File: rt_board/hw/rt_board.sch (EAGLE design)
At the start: 66 parts, among them IC1 MCP170333MB, IC2/L1 TLE4935L, IC3/L2 TLE4935L, IC4/L1 TLE4935L, IC5/L2 TLE4935L, Q1 8MHz, SW1 B3U-1000PM-B, SW2 B3U-1000PM-B, U1 STM32F051R8T7, U2 SN74AVC4T245PW, U3 DRV8801PWP, U4 ACS712ELCTR-05B-T, U5 DRV8801PWP, U6 ACS712ELCTR-05B-T, U7 2N7002BKW, X1 PWR, X2 LEFT, X3 RIGHT

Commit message: first PCB/SMD version
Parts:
- removed D3: BZX84CSMD, diode:BZX84CSMD
- C12: value 100uF -> 100nF; device rcl:CPOL-EU153CLV-0810 -> rcl:C-EUC1206
- C14: value 1nF -> 20pF; device rcl:C-EUC1206 -> rcl:C-EUC0603
- C15: value 100nF -> 100uF; device rcl:C-EUC1206 -> rcl:CPOL-EU153CLV-0605
- C16: value 100nF -> 20pF; device rcl:C-EUC1206 -> rcl:C-EUC0603
- C18: value 100uF -> 4.7uF; device rcl:CPOL-EU153CLV-0810 -> rcl:CPOL-EU153CLV-0405
- C2: value 4.7uF -> 100nF; device rcl:CPOL-EU153CLV-0405 -> rcl:C-EUC1206
- C20: value 1nF -> 100nF
- C22: value 100nF -> 4.7uF; device rcl:C-EUC1206 -> rcl:CPOL-EU153CLV-0405
- C3: device rcl:CPOL-EU153CLV-0605 -> rcl:CPOL-EU153CLV-0810
- C4: value 4.7uF -> 100uF; device rcl:CPOL-EU153CLV-0405 -> rcl:CPOL-EU153CLV-0810
- C7: value 100nF -> 1nF
- C8: value 20pF -> 1nF; device rcl:C-EUC0603 -> rcl:C-EUC1206
- C9: value 20pF -> 100nF; device rcl:C-EUC0603 -> rcl:C-EUC1206
- D1: value CGRM4001-G -> BZX84CSMD; device diode:CGRM4001-G -> diode:BZX84CSMD
- R1, R2: value 1kR -> 2kR
- R10: value 3kR -> 3.3kR
- R11: value 3.3kR -> 350mA; device rcl:R-EU_R0603 -> rcl:R-EU_MELF0204W
- R12: value 2kR -> 350mA; device rcl:R-EU_R0603 -> rcl:R-EU_MELF0204W
- R13: value 3kR -> 1kR
- R14: value 2kR -> 1kR
- R15: value 3kR -> 100kR
- R16: value 3.3kR -> 100kR
- R3, R4: value 100kR -> 2kR
- R5, R6: value 350mA -> 3kR; device rcl:R-EU_MELF0204W -> rcl:R-EU_R0603
- R7: value 2kR -> 3kR
- R9: value 2kR -> 3.3kR
- U1: value STM32F051R8T7 -> DRV8801PWP; device stm32f51r8r6:STM32F051R8T6 -> TI-DRV8801PWP:DRV8801PWP
- U2: value SN74AVC4T245PW -> DRV8801PWP; device TI-SN74AVC4T245PW:SN74AVC4T245PW -> TI-DRV8801PWP:DRV8801PWP
- U3: value DRV8801PWP -> SN74AVC4T245PW; device TI-DRV8801PWP:DRV8801PWP -> TI-SN74AVC4T245PW:SN74AVC4T245PW
- U5: value DRV8801PWP -> ACS712ELCTR-05B-T; device TI-DRV8801PWP:DRV8801PWP -> Allegro-ACS712ELCTR-20A-T:ACS712ELCTR-20A-T
- U6: value ACS712ELCTR-05B-T -> STM32F051R8T7; device Allegro-ACS712ELCTR-20A-T:ACS712ELCTR-20A-T -> stm32f51r8r6:STM32F051R8T6
- X1: value PWR -> LEFT
- X2: value LEFT -> RIGHT
- X3: value RIGHT -> PWR
- renumbered IC3/L2 to IC3/L1, IC5/L2 to IC5/L1
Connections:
- removed net N$1: C3.+, D1.C, IC1.VI1
- net +12V: now also C1.1, C12.1, C2.1, C3.+, C4.+, U1.VBB, U2.VBB; no longer C12.+, C15.1, C17.1, C18.+, C21.1, U3.VBB, U5.VBB
- net +5V: now also C18.+, C19.1, C20.1, C21.1, C22.+, R14.1, R15.2, U3.VCCB, U6.VBAT, U6.VDD, U6.VDD_2; no longer C1.1, C2.+, C4.+, C5.1, C6.1, R2.1, R4.2, U1.VBAT, U1.VDD, U1.VDD_2, U2.VCCB
- net +5V/1: now also C15.+, C5.1, C6.1, IC1.VI1, R12.2, U5.VCC; no longer C13.1, C19.1, D1.A, R6.2, U6.VCC
- net +5V/4: now also R10.2, R11.1, R9.2, U3.1DIR, U3.VCCA; no longer R11.2, R16.2, R5.1, U2.1DIR, U2.VCCA
- net 0V: now also C15.-, C16.2, C2.2, C21.2, C22.-, D1.A, R13.1, R16.1, R5.2, R6.2, R7.2, U1.EP, U1.GND, U1.GND_2, U1.MODE_2, U2.EP, U2.MODE_2, U3.1~OE, U3.2DIR, U3.2~OE, U5.IP-, U5.IP-_2, U6.VSS, U6.VSSA, U6.VSS_2, X3-2.KL; no longer C10.2, C11.2, C12.-, C2.-, C9.2, D3.A, R1.1, R10.2, R13.2, R15.2, R3.1, U1.VSS, U1.VSSA, U1.VSS_2, U2.1~OE, U2.2DIR, U2.2~OE, U3.EP, U3.MODE_2, U5.EP, U5.GND_2, U5.MODE_2, U6.GND, U6.IP-, U6.IP-_2, X1-2.KL
- net N$10: now also R12.1; no longer R6.1
- net N$11: now also R11.2; no longer R5.2
- net N$12: now also U3.1A1; no longer U2.1A1
- net N$13: now also U3.1B1, U6.PA3; no longer U1.PA3, U2.1B1
- net N$14: now also U3.2B1, U6.PA2; no longer U1.PA2, U2.2B1
- net N$15: now also U3.2A1; no longer U2.2A1
- net N$16: now also R1.1; no longer R7.1
- net N$17: now also R1.2, R5.1, U6.PA8; no longer R7.2, R8.1, U1.PA8
- net N$18: now also R2.1; no longer R9.1
- net N$19: now also R2.2, R6.1, U6.PA9; no longer R10.1, R9.2, U1.PA9
- net N$2: now also X3-1.KL; no longer X1-1.KL
- net N$20: now also U1.OUT+, X1-1.KL; no longer U3.OUT+, X2-1.KL
- net N$21: now also U1.OUT-, X1-2.KL; no longer U3.OUT-, X2-2.KL
- net N$22: now also U1.SENSE; no longer U3.SENSE
- net N$23: now also D1.C, U6.PA4; no longer D2.C, U1.PA4
- net N$24: now also C7.1; no longer C14.1
- net N$25: now also R9.1, U1.NSLEEP; no longer R11.1, U3.NSLEEP
- net N$26: now also C11.2, U1.VCP; no longer C15.2, U3.VCP
- net N$27: now also C9.2, U1.CP2; no longer C16.2, U3.CP2
- net N$28: now also C9.1, U1.CP1; no longer C16.1, U3.CP1
- net N$29: now also R3.1; no longer R12.1
- net N$3: now also C17.1, U6.VDDA; no longer C10.1, U1.VDDA
- net N$30: now also R3.2, R7.1, U6.PB4; no longer R12.2, R13.1, U1.PB4
- net N$31: now also R4.1; no longer R14.1
- net N$32: now also R4.2, R8.1, U6.PB5; no longer R14.2, R15.1, U1.PB5
- net N$33: now also U2.OUT+, X2-1.KL; no longer U5.OUT+, X3-1.KL
- net N$34: now also U2.OUT-, X2-2.KL; no longer U5.OUT-, X3-2.KL
- net N$35: now also C8.1, U5.FILTER; no longer C20.1, U6.FILTER
- net N$36: now also U2.SENSE, U5.IP+, U5.IP+_2; no longer U5.SENSE, U6.IP+, U6.IP+_2
- net N$37: now also D2.C, U5.VIOUT, U6.PA5; no longer D3.C, U1.PA5, U6.VIOUT
- net N$38: now also R10.1, U2.NSLEEP; no longer R16.1, U5.NSLEEP
- net N$39: now also C12.2, U2.VCP; no longer C21.2, U5.VCP
- net N$4: now also R16.2, U6.PA14(SWCLK); no longer R3.2, U1.PA14(SWCLK)
- net N$40: now also C10.2, U2.CP2; no longer C22.2, U5.CP2
- net N$41: now also C10.1, U2.CP1; no longer C22.1, U5.CP1
- net N$42: now also U1.MODE_1, U2.MODE_1, U6.PB13; no longer U1.PB13, U3.MODE_1, U5.MODE_1
- net N$44: now also U6.PB0; no longer U1.PB0
- net N$45: now also U1.ENABLE, U6.PB14; no longer U1.PB14, U3.ENABLE
- net N$46: now also U2.ENABLE, U6.PB15; no longer U1.PB15, U5.ENABLE
- net N$48: now also U1.PHASE, U6.PB12; no longer U1.PB12, U3.PHASE
- net N$49: now also U2.PHASE, U6.PB11; no longer U1.PB11, U5.PHASE
- net N$5: now also R13.2, U6.BOOT0; no longer R1.2, U1.BOOT0
- net N$6: now also C13.1, R14.2, U6.NRST; no longer C7.1, R2.2, U1.NRST
- net N$7: now also C14.1, U6.PF0-OSC_IN; no longer C8.1, U1.PF0-OSC_IN
- net N$8: now also C16.1, U6.PF1-OSC_OUT; no longer C9.1, U1.PF1-OSC_OUT
- net N$9: now also R15.1, U6.PA13(SWDAT); no longer R4.1, U1.PA13(SWDAT)
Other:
- moved on the sheet: C1, C10, C11, C13, C14, C16, C17, C18, C19, C20, C21, C3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

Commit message: minor fixes suggested by the tool
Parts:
- SV2: value (none) -> SWD
- renumbered SWD to SV2
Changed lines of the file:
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@@
 <part name="C17" library="rcl" deviceset="C-EU" device="C1206" value="100nF"/>
 <part name="SUPPLY22" library="supply2" deviceset="0V" device=""/>
-<part name="SWD" library="con-lstb" deviceset="MA06-1" device=""/>
+<part name="SV2" library="con-lstb" deviceset="MA06-1" device="" value="SWD"/>
 <part name="SUPPLY23" library="supply2" deviceset="0V" device=""/>
 <part name="SUPPLY34" library="supply2" deviceset="+5V" device="" value="+3.3V"/>
@@
 <instance part="C17" gate="G$1" x="-40.64" y="104.14"/>
 <instance part="SUPPLY22" gate="0V" x="-40.64" y="93.98"/>
-<instance part="SWD" gate="1" x="-88.9" y="5.08"/>
+<instance part="SV2" gate="1" x="-88.9" y="5.08"/>
 <instance part="SUPPLY23" gate="0V" x="-73.66" y="-10.16"/>
 <instance part="SUPPLY34" gate="+5V" x="-78.74" y="-7.62"/>
@@
 <instance part="SUPPLY30" gate="0V" x="-195.58" y="48.26"/>
 <instance part="SUPPLY31" gate="0V" x="-198.12" y="50.8"/>
-<instance part="SUPPLY2" gate="G$1" x="-58.42" y="152.4"/>
+<instance part="SUPPLY2" gate="G$1" x="-63.5" y="152.4"/>
 <instance part="SUPPLY28" gate="0V" x="-198.12" y="66.04"/>
 <instance part="SUPPLY25" gate="G$1" x="-205.74" y="63.5"/>
@@
 <pinref part="SUPPLY9" gate="0V" pin="0V"/>
 <junction x="30.48" y="137.16"/>
+<junction x="35.56" y="137.16"/>
+<junction x="25.4" y="137.16"/>
 </segment>
 <segment>
@@
 </segment>
 <segment>
-<pinref part="SWD" gate="1" pin="3"/>
+<pinref part="SV2" gate="1" pin="3"/>
 <pinref part="SUPPLY23" gate="0V" pin="0V"/>
 <wire x1="-73.66" y1="-7.62" x2="-73.66" y2="2.54" width="0.1524" layer="91"/>
@@
 <pinref part="SUPPLY8" gate="+5V" pin="+5V"/>
 <junction x="30.48" y="144.78"/>
+<junction x="25.4" y="144.78"/>
+<junction x="35.56" y="144.78"/>
 </segment>
 <segment>
@@
 </segment>
 <segment>
-<pinref part="SWD" gate="1" pin="1"/>
+<pinref part="SV2" gate="1" pin="1"/>
 <pinref part="SUPPLY34" gate="+5V" pin="+5V"/>
 <wire x1="-78.74" y1="-10.16" x2="-81.28" y2="-10.16" width="0.1524" layer="91"/>
@@
 <pinref part="SW1" gate="G$1" pin="P$1"/>
 <wire x1="-104.14" y1="76.2" x2="-104.14" y2="71.12" width="0.1524" layer="91"/>
+<junction x="-104.14" y="71.12"/>
 </segment>
 </net>
@@
 <pinref part="C13" gate="G$1" pin="1"/>
 <junction x="-68.58" y="93.98"/>
-<pinref part="SWD" gate="1" pin="5"/>
+<pinref part="SV2" gate="1" pin="5"/>
 <wire x1="-81.28" y1="7.62" x2="-76.2" y2="7.62" width="0.1524" layer="91"/>
 <wire x1="-76.2" y1="7.62" x2="-76.2" y2="93.98" width="0.1524" layer="91"/>
@@
 <net name="N$4" class="0">
 <segment>
-<pinref part="SWD" gate="1" pin="2"/>
+<pinref part="SV2" gate="1" pin="2"/>
 <wire x1="-81.28" y1="0" x2="-48.26" y2="0" width="0.1524" layer="91"/>
 <wire x1="-48.26" y1="0" x2="-48.26" y2="7.62" width="0.1524" layer="91"/>
@@
 <wire x1="-50.8" y1="10.16" x2="-50.8" y2="5.08" width="0.1524" layer="91"/>
 <wire x1="-50.8" y1="5.08" x2="-58.42" y2="5.08" width="0.1524" layer="91"/>
-<pinref part="SWD" gate="1" pin="4"/>
+<pinref part="SV2" gate="1" pin="4"/>
 <wire x1="-58.42" y1="5.08" x2="-81.28" y2="5.08" width="0.1524" layer="91"/>
 <pinref part="R15" gate="G$1" pin="1"/>
@@
 <pinref part="SUPPLY2" gate="G$1" pin="+5V/1"/>
 <junction x="-58.42" y="149.86"/>
+<wire x1="-58.42" y1="149.86" x2="-63.5" y2="149.86" width="0.1524" layer="91"/>
 </segment>
 </net>
@@
 <pinref part="U6" gate="A" pin="PB4"/>
 <wire x1="30.48" y1="2.54" x2="20.32" y2="2.54" width="0.1524" layer="91"/>
+<junction x="-187.96" y="-137.16"/>
 </segment>
 </net>
@@
 <pinref part="U6" gate="A" pin="PB5"/>
 <wire x1="27.94" y1="0" x2="20.32" y2="0" width="0.1524" layer="91"/>
+<junction x="-187.96" y="-157.48"/>
 </segment>
 </net>
@@
 </sheet>
 </sheets>
+<errors>
+</errors>
 </schematic>
 </drawing>

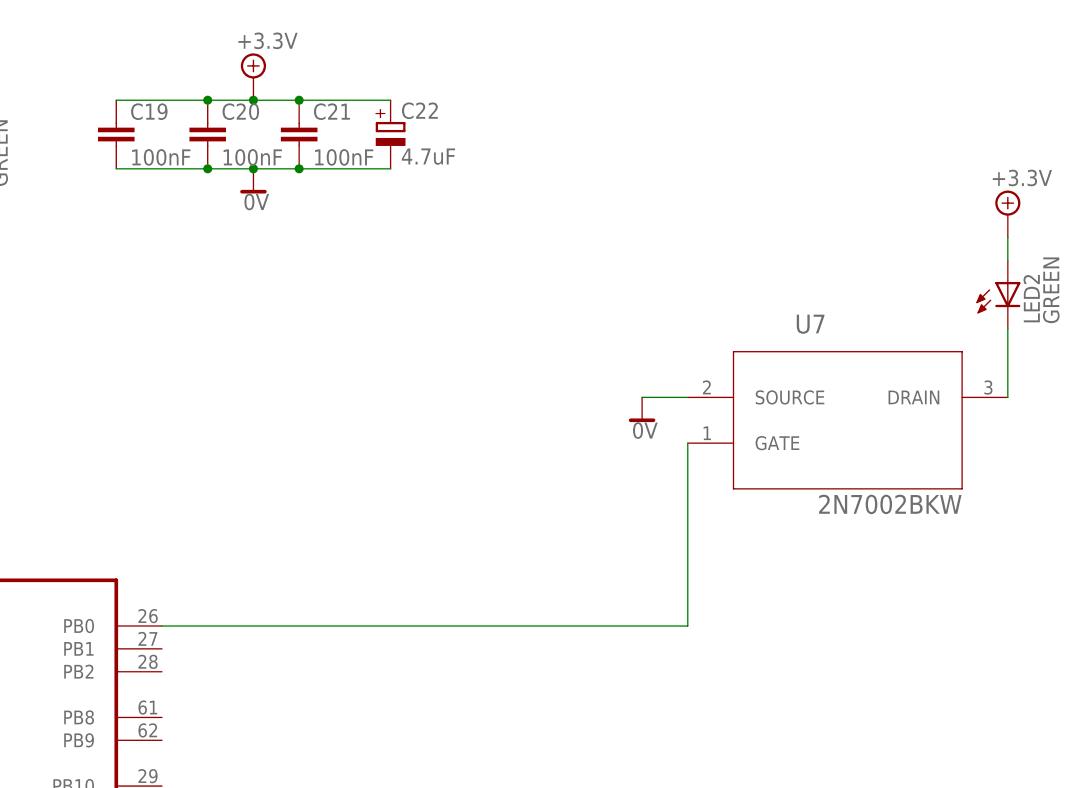
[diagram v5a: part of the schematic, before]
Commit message: fixed and simplified user-defined LED-1 control
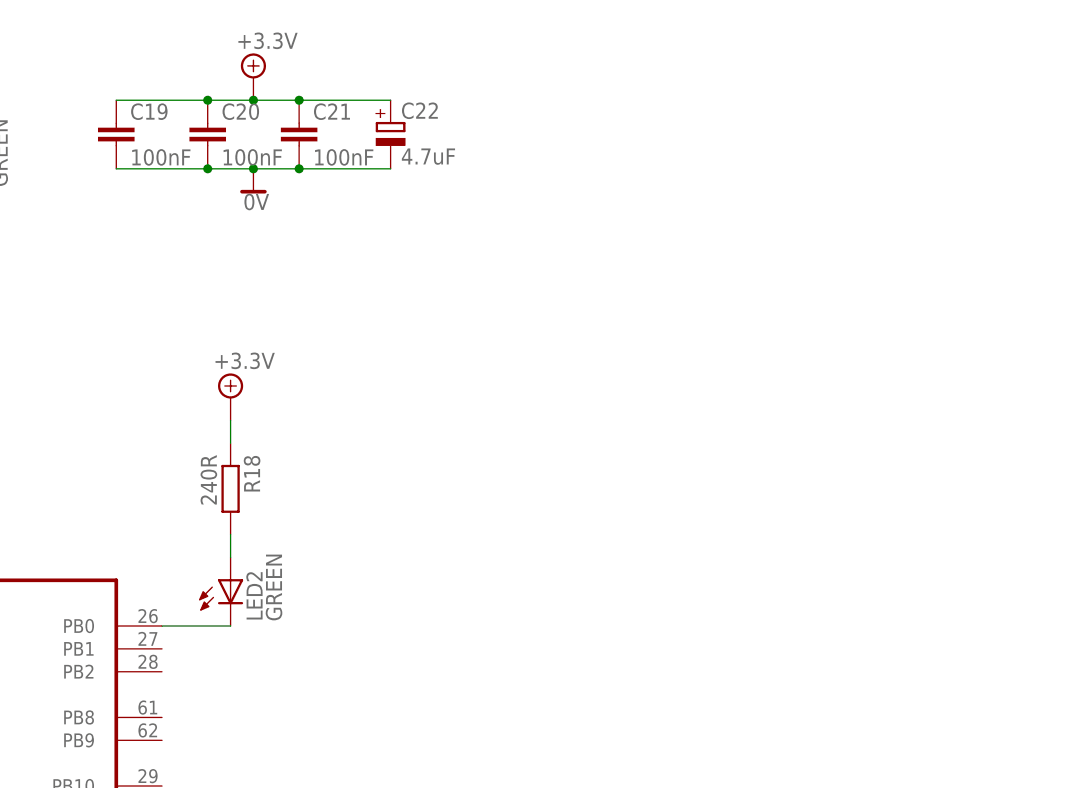
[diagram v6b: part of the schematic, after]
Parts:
- removed U7: 2N7002BKW, 2n7002:2N7002BKW
- added R18: 240R, rcl:R-EU_R0603
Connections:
- removed net N$47: LED2.C, U7.DRAIN
- new net N$1: LED2.C, U6.PB0
- net +5V: now also R18.1; no longer LED2.A
- net 0V: no longer U7.SOURCE
- net N$44: now also LED2.A, R18.2; no longer U6.PB0, U7.GATE
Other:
- moved on the sheet: LED2
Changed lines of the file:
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@@
 <part name="SUPPLY59" library="supply2" deviceset="+5V" device="" value="+3.3V"/>
 <part name="SUPPLY80" library="supply2" deviceset="0V" device=""/>
-<part name="U7" library="2n7002" deviceset="2N7002BKW" device=""/>
-<part name="SUPPLY83" library="supply2" deviceset="0V" device=""/>
 <part name="LED2" library="led" deviceset="LED" device="CHIPLED_0603" value="GREEN"/>
 <part name="SUPPLY84" library="supply2" deviceset="+5V" device="" value="+3.3V"/>
@@
 <part name="SUPPLY85" library="supply2" deviceset="+5V" device="" value="+3.3V"/>
 <part name="SUPPLY86" library="supply2" deviceset="0V" device=""/>
+<part name="R18" library="rcl" deviceset="R-EU_" device="R0603" value="240R"/>
 </parts>
 <sheets>
@@
 <instance part="SUPPLY59" gate="+5V" x="-2.54" y="160.02"/>
 <instance part="SUPPLY80" gate="0V" x="-2.54" y="129.54"/>
-<instance part="U7" gate="A" x="78.74" y="111.76"/>
-<instance part="SUPPLY83" gate="0V" x="73.66" y="109.22"/>
-<instance part="LED2" gate="G$1" x="114.3" y="124.46"/>
-<instance part="SUPPLY84" gate="+5V" x="114.3" y="132.08"/>
+<instance part="LED2" gate="G$1" x="27.94" y="91.44"/>
+<instance part="SUPPLY84" gate="+5V" x="27.94" y="111.76"/>
 <instance part="SW1" gate="G$1" x="-104.14" y="83.82" rot="R90"/>
 <instance part="SW2" gate="G$1" x="-86.36" y="86.36" rot="R90"/>
 <instance part="SUPPLY85" gate="+5V" x="-104.14" y="96.52"/>
 <instance part="SUPPLY86" gate="0V" x="-83.82" y="76.2"/>
+<instance part="R18" gate="G$1" x="27.94" y="101.6" rot="R270"/>
 </instances>
 <busses>
@@
 </segment>
 <segment>
-<pinref part="U7" gate="A" pin="SOURCE"/>
-<pinref part="SUPPLY83" gate="0V" pin="0V"/>
-<wire x1="73.66" y1="111.76" x2="78.74" y2="111.76" width="0.1524" layer="91"/>
-</segment>
-<segment>
 <pinref part="SW2" gate="G$1" pin="P$1"/>
 <pinref part="SUPPLY86" gate="0V" pin="0V"/>
@@
 </segment>
 <segment>
-<pinref part="LED2" gate="G$1" pin="A"/>
-<pinref part="SUPPLY84" gate="+5V" pin="+5V"/>
-<wire x1="114.3" y1="129.54" x2="114.3" y2="127" width="0.1524" layer="91"/>
-</segment>
-<segment>
 <pinref part="SW1" gate="G$1" pin="P$2"/>
 <pinref part="SUPPLY85" gate="+5V" pin="+5V"/>
 <wire x1="-104.14" y1="91.44" x2="-104.14" y2="93.98" width="0.1524" layer="91"/>
+</segment>
+<segment>
+<pinref part="R18" gate="G$1" pin="1"/>
+<pinref part="SUPPLY84" gate="+5V" pin="+5V"/>
+<wire x1="27.94" y1="109.22" x2="27.94" y2="106.68" width="0.1524" layer="91"/>
 </segment>
 </net>
@@
 </segment>
 </net>
+<net name="N$1" class="0">
+<segment>
+<pinref part="U6" gate="A" pin="PB0"/>
+<pinref part="LED2" gate="G$1" pin="C"/>
+<wire x1="27.94" y1="86.36" x2="20.32" y2="86.36" width="0.1524" layer="91"/>
+</segment>
+</net>
 <net name="N$44" class="0">
 <segment>
-<pinref part="U6" gate="A" pin="PB0"/>
-<pinref part="U7" gate="A" pin="GATE"/>
-<wire x1="20.32" y1="86.36" x2="78.74" y2="86.36" width="0.1524" layer="91"/>
-<wire x1="78.74" y1="86.36" x2="78.74" y2="106.68" width="0.1524" layer="91"/>
-</segment>
-</net>
-<net name="N$47" class="0">
-<segment>
-<pinref part="U7" gate="A" pin="DRAIN"/>
-<pinref part="LED2" gate="G$1" pin="C"/>
-<wire x1="114.3" y1="119.38" x2="114.3" y2="111.76" width="0.1524" layer="91"/>
-</segment>
-</net>
+<pinref part="LED2" gate="G$1" pin="A"/>
+<pinref part="R18" gate="G$1" pin="2"/>
+<wire x1="27.94" y1="96.52" x2="27.94" y2="93.98" width="0.1524" layer="91"/>
+</segment>
+</net>

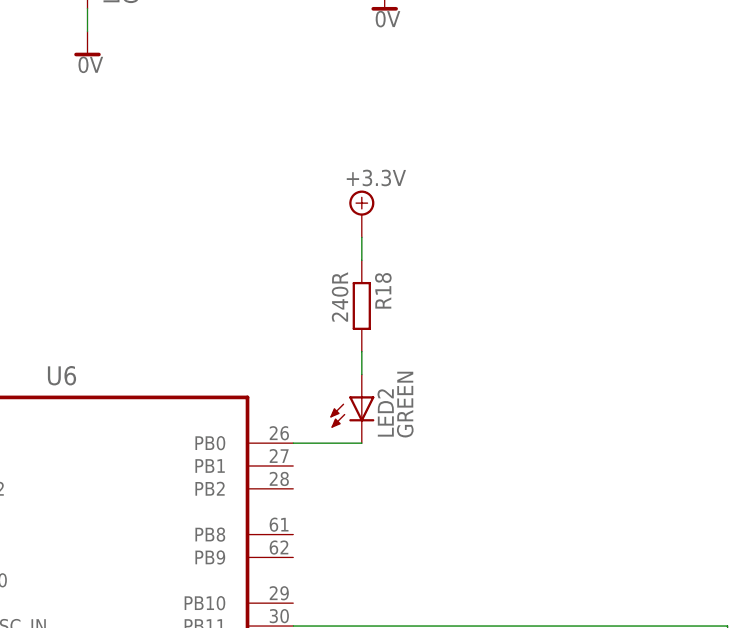
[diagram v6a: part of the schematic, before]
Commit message: added user LED 2
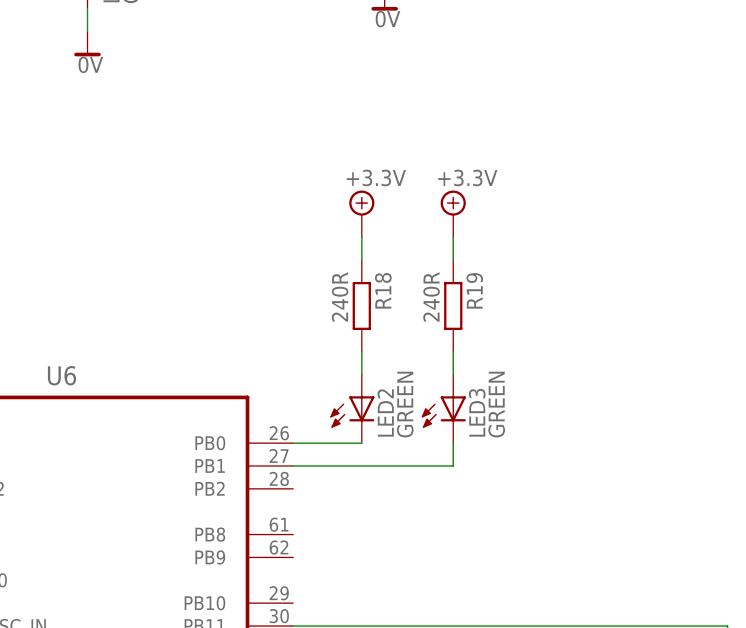
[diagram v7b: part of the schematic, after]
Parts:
- added LED3: GREEN, led:LEDCHIPLED_0603
- added R19: 240R, rcl:R-EU_R0603
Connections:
- new net N$47: LED3.C, U6.PB1
- new net N$51: LED3.A, R19.2
- net +5V: now also R19.1
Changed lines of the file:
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@@
 <part name="SUPPLY86" library="supply2" deviceset="0V" device=""/>
 <part name="R18" library="rcl" deviceset="R-EU_" device="R0603" value="240R"/>
+<part name="LED3" library="led" deviceset="LED" device="CHIPLED_0603" value="GREEN"/>
+<part name="R19" library="rcl" deviceset="R-EU_" device="R0603" value="240R"/>
+<part name="SUPPLY83" library="supply2" deviceset="+5V" device="" value="+3.3V"/>
 </parts>
 <sheets>
@@
 <instance part="SUPPLY86" gate="0V" x="-83.82" y="76.2"/>
 <instance part="R18" gate="G$1" x="27.94" y="101.6" rot="R270"/>
+<instance part="LED3" gate="G$1" x="38.1" y="91.44"/>
+<instance part="R19" gate="G$1" x="38.1" y="101.6" rot="R270"/>
+<instance part="SUPPLY83" gate="+5V" x="38.1" y="111.76"/>
 </instances>
 <busses>
@@
 <pinref part="SUPPLY84" gate="+5V" pin="+5V"/>
 <wire x1="27.94" y1="109.22" x2="27.94" y2="106.68" width="0.1524" layer="91"/>
+</segment>
+<segment>
+<pinref part="R19" gate="G$1" pin="1"/>
+<pinref part="SUPPLY83" gate="+5V" pin="+5V"/>
+<wire x1="38.1" y1="109.22" x2="38.1" y2="106.68" width="0.1524" layer="91"/>
 </segment>
 </net>
@@
 </segment>
 </net>
+<net name="N$47" class="0">
+<segment>
+<pinref part="U6" gate="A" pin="PB1"/>
+<pinref part="LED3" gate="G$1" pin="C"/>
+<wire x1="38.1" y1="86.36" x2="38.1" y2="83.82" width="0.1524" layer="91"/>
+<wire x1="38.1" y1="83.82" x2="20.32" y2="83.82" width="0.1524" layer="91"/>
+</segment>
+</net>
+<net name="N$51" class="0">
+<segment>
+<pinref part="LED3" gate="G$1" pin="A"/>
+<pinref part="R19" gate="G$1" pin="2"/>
+<wire x1="38.1" y1="96.52" x2="38.1" y2="93.98" width="0.1524" layer="91"/>
+</segment>
+</net>
